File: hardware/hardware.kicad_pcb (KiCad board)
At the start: 4 copper layers, 0 parts

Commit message: atualizando alguns footprints; começando o desenho da placa
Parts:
- added ANT1: PCB_ANT, RF_Antenna:Texas_SWRA117D_2.4GHz_Left, F.Cu at (72.3, 25.4)
- added C1: TBD, Capacitor_SMD:C_0402_1005Metric, F.Cu at (46.5, 20.3)
- added C10: 1uF, Capacitor_SMD:C_0402_1005Metric, F.Cu at (136.1, 82.4)
- added C11: 0.1uF, Capacitor_SMD:C_0402_1005Metric, F.Cu at (46.5, 36.0)
- added C12: 10nF, Capacitor_SMD:C_0402_1005Metric, F.Cu at (136.1, 83.7)
- added C13: 10pF, Capacitor_SMD:C_0402_1005Metric, F.Cu at (49.4, 22.2)
- added C14: 10pF, Capacitor_SMD:C_0402_1005Metric, F.Cu at (49.4, 24.2)
- added C15: 100nF, Capacitor_SMD:C_0805_2012Metric_Pad1.18x1.45mm_HandSolder, F.Cu at (73.5, 44.5)
- added C16: 0.1uF, Capacitor_SMD:C_0402_1005Metric, F.Cu at (49.4, 26.2)
- added C17: 22uF, Capacitor_SMD:C_0603_1608Metric_Pad1.08x0.95mm_HandSolder, F.Cu at (47.2, 52.5)
- added C18: TBD, Capacitor_SMD:C_0402_1005Metric, F.Cu at (49.4, 28.1)
- added C19: TBD, Capacitor_SMD:C_0402_1005Metric, F.Cu at (49.4, 30.1)
- added C2: TBD, Capacitor_SMD:C_0402_1005Metric, F.Cu at (46.5, 22.2)
- added C20: 22uF, Capacitor_SMD:C_0603_1608Metric_Pad1.08x0.95mm_HandSolder, F.Cu at (47.2, 55.0)
- added C21: 22uF, Capacitor_SMD:C_0603_1608Metric_Pad1.08x0.95mm_HandSolder, F.Cu at (47.2, 57.5)
- added C22: 0.1uF, Capacitor_SMD:C_0402_1005Metric, F.Cu at (49.4, 32.1)
- added C23: 0.1uF, Capacitor_SMD:C_0402_1005Metric, F.Cu at (49.4, 34.0)
- added C24: 1uF, Capacitor_SMD:C_0402_1005Metric, F.Cu at (49.4, 36.0)
- added C25: 1uF, Capacitor_SMD:C_0402_1005Metric, F.Cu at (162.4, 129.5)
- added C26: 1uF, Capacitor_SMD:C_0402_1005Metric, F.Cu at (162.3, 125.1)
- added C27: 1uF, Capacitor_SMD:C_0402_1005Metric, F.Cu at (164.0, 125.1)
- added C28: 100nF, Capacitor_SMD:C_0402_1005Metric, F.Cu at (52.2, 26.2)
- added C29: 220nF, Capacitor_SMD:C_0402_1005Metric, F.Cu at (174.8, 129.0)
- added C3: 1uF, Capacitor_SMD:C_0402_1005Metric, F.Cu at (127.0, 87.0)
- added C30: 1uF, Capacitor_SMD:C_0402_1005Metric, F.Cu at (175.3, 123.1)
- added C31: 220nF, Capacitor_SMD:C_0402_1005Metric, F.Cu at (175.7, 124.4)
- added C32: 220nF, Capacitor_SMD:C_0402_1005Metric, F.Cu at (186.8, 129.3)
- added C33: 220nF, Capacitor_SMD:C_0402_1005Metric, F.Cu at (174.8, 127.1)
- added C34: 100nF, Capacitor_SMD:C_0402_1005Metric, F.Cu at (55.1, 20.3)
- added C35: 470nF, Capacitor_SMD:C_0402_1005Metric, F.Cu at (110.2, 103.3)
- added C36: 470nF, Capacitor_SMD:C_0402_1005Metric, F.Cu at (110.2, 105.3)
- added C37: 100nF, Capacitor_SMD:C_0402_1005Metric, F.Cu at (110.2, 107.2)
- added C38: 470uF, Capacitor_SMD:C_0402_1005Metric, F.Cu at (110.2, 109.2)
- added C39: 100nF, Capacitor_SMD:C_0402_1005Metric, F.Cu at (110.2, 111.2)
- added C4: TBD, Capacitor_SMD:C_0402_1005Metric, F.Cu at (46.5, 26.2)
- added C40: 1nF, Capacitor_SMD:C_0402_1005Metric, F.Cu at (110.2, 113.2)
- added C41: 1nF, Capacitor_SMD:C_0402_1005Metric, F.Cu at (110.2, 115.1)
- added C42: 100nF, Capacitor_SMD:C_0402_1005Metric, F.Cu at (55.1, 36.0)
- added C43: 10nF, Capacitor_SMD:C_0402_1005Metric, F.Cu at (113.0, 101.3)
- added C44: 10nF, Capacitor_SMD:C_0402_1005Metric, F.Cu at (113.0, 103.3)
- added C45: 100nF, Capacitor_SMD:C_0402_1005Metric, F.Cu at (58.0, 24.2)
- added C46: 100nF, Capacitor_SMD:C_0402_1005Metric, F.Cu at (58.0, 26.2)
- added C5: 10nF, Capacitor_SMD:C_0402_1005Metric, F.Cu at (128.5, 87.0)
- added C6: 10uF, Capacitor_SMD:C_0805_2012Metric_Pad1.18x1.45mm_HandSolder, F.Cu at (73.5, 38.5)
- added C7: 0.1uF, Capacitor_SMD:C_0402_1005Metric, F.Cu at (130.0, 87.0)
- added C8: 10uF, Capacitor_SMD:C_0805_2012Metric_Pad1.18x1.45mm_HandSolder, F.Cu at (73.5, 41.5)
- added C9: 0.1uF, Capacitor_SMD:C_0402_1005Metric, F.Cu at (134.0, 87.1)
- added D1: LED_ARGB, Connector_PinHeader_1.27mm:PinHeader_1x04_P1.27mm_Vertical_SMD_Pin1Left, F.Cu at (63.4, 29.9)
- added IC1: TAS5760LDAPR, Package_SO:HTSSOP-32-1EP_6.1x11mm_P0.65mm_EP5.2x11mm_Mask4.11x4.36mm_ThermalVias, F.Cu at (169.5, 128.0)
- added J2: Conn_01x04, Connector_PinHeader_1.27mm:PinHeader_1x04_P1.27mm_Vertical, F.Cu at (67.1, 55.2)
- added J3: Conn_01x04, Connector_PinHeader_1.27mm:PinHeader_1x04_P1.27mm_Vertical, F.Cu at (71.3, 55.2)
- added JP1: SolderJumper_2_Open, Jumper:SolderJumper-2_P1.3mm_Open_RoundedPad1.0x1.5mm, F.Cu at (102.3, 119.9)
- added JP2: SolderJumper_2_Open, Jumper:SolderJumper-2_P1.3mm_Open_RoundedPad1.0x1.5mm, F.Cu at (102.3, 123.4)
- added JP3: SolderJumper_2_Open, Jumper:SolderJumper-2_P1.3mm_Open_RoundedPad1.0x1.5mm, F.Cu at (102.3, 127.0)
- added JP4: SolderJumper_2_Open, Jumper:SolderJumper-2_P1.3mm_Open_RoundedPad1.0x1.5mm, F.Cu at (102.3, 130.5)
- added L1: TBD, Inductor_SMD:L_0402_1005Metric, F.Cu at (60.9, 38.0)
- added L2: TBD, Inductor_SMD:L_0402_1005Metric, F.Cu at (60.9, 40.0)
- added L3: 2.0nH (0.1nH), Inductor_SMD:L_0402_1005Metric, F.Cu at (132.0, 86.6)
- added L4: 2.2uH, Inductor_SMD:L_TDK_VLS6045EX_VLS6045AF, F.Cu at (71.3, 30.1)
- added L5: 10uH, Inductor_SMD:L_0402_1005Metric, F.Cu at (116.0, 125.0)
- added L6: 10uH, Inductor_SMD:L_0402_1005Metric, F.Cu at (116.0, 127.0)
- added LS1: 4R, Connector_PinSocket_2.54mm:PinSocket_2x01_P2.54mm_Vertical_SMD, F.Cu at (125.2, 132.3)
- added R1: 49.9K, Resistor_SMD:R_0402_1005Metric, F.Cu at (60.9, 47.9)
- added R10: 10K, Resistor_SMD:R_0201_0603Metric_Pad0.64x0.40mm_HandSolder, F.Cu at (60.9, 51.6)
- added R11: 10K, Resistor_SMD:R_0201_0603Metric_Pad0.64x0.40mm_HandSolder, F.Cu at (163.8, 126.4)
- added R12: 10K, Resistor_SMD:R_0201_0603Metric_Pad0.64x0.40mm_HandSolder, F.Cu at (163.9, 128.4)
- added R13: 10K, Resistor_SMD:R_0201_0603Metric_Pad0.64x0.40mm_HandSolder, F.Cu at (163.9, 129.6)
- added R14: R, Resistor_SMD:R_0201_0603Metric_Pad0.64x0.40mm_HandSolder, F.Cu at (163.9, 127.6)
- added R15: R, Resistor_SMD:R_0201_0603Metric_Pad0.64x0.40mm_HandSolder, F.Cu at (163.8, 132.2)
- added R16: 10K, Resistor_SMD:R_0201_0603Metric_Pad0.64x0.40mm_HandSolder, F.Cu at (60.9, 58.6)
- added R17: 560R, Resistor_SMD:R_0402_1005Metric, F.Cu at (66.7, 44.0)
- added R18: 560R, Resistor_SMD:R_0402_1005Metric, F.Cu at (66.7, 46.0)
- added R19: 560R, Resistor_SMD:R_0402_1005Metric, F.Cu at (66.7, 47.9)
- added R2: 49.9K, Resistor_SMD:R_0402_1005Metric, F.Cu at (63.8, 38.0)
- added R20: 10K, Resistor_SMD:R_0201_0603Metric_Pad0.64x0.40mm_HandSolder, F.Cu at (63.7, 49.8)
- added R21: 1K, Resistor_SMD:R_0402_1005Metric, F.Cu at (69.6, 38.0)
- added R22: 10K, Resistor_SMD:R_0201_0603Metric_Pad0.64x0.40mm_HandSolder, F.Cu at (63.7, 51.6)
- added R23: 3.3R, Resistor_SMD:R_0402_1005Metric, F.Cu at (124.7, 121.1)
- added R24: 3.3R, Resistor_SMD:R_0402_1005Metric, F.Cu at (124.7, 123.1)
- added R25: 1K, Resistor_SMD:R_0402_1005Metric, F.Cu at (69.6, 44.0)
- added R26: 10K, Resistor_SMD:R_0201_0603Metric_Pad0.64x0.40mm_HandSolder, F.Cu at (63.7, 53.3)
- added R27: 10K, Resistor_SMD:R_0201_0603Metric_Pad0.64x0.40mm_HandSolder, F.Cu at (63.7, 55.1)
- added R3: 49.9K, Resistor_SMD:R_0402_1005Metric, F.Cu at (63.8, 40.0)
- added R4: 49.9K, Resistor_SMD:R_0402_1005Metric, F.Cu at (63.8, 42.0)
- added R5: 10K, Resistor_SMD:R_0201_0603Metric_Pad0.64x0.40mm_HandSolder, F.Cu at (60.9, 49.8)
- added R6: 0R, Resistor_SMD:R_0402_1005Metric, F.Cu at (63.8, 44.0)
- added R7: TBD, Resistor_SMD:R_0402_1005Metric, F.Cu at (63.8, 46.0)
- added R8: 499R, Resistor_SMD:R_0402_1005Metric, F.Cu at (63.8, 47.9)
- added R9: 33.2K, Resistor_SMD:R_0402_1005Metric, F.Cu at (66.7, 38.0)
- added SW1: SW_Push, Button_Switch_SMD:SW_SPST_PTS810, F.Cu at (41.7, 21.6)
- added SW2: SW_Push, Button_Switch_SMD:SW_SPST_PTS810, F.Cu at (41.7, 26.4)
- added SW3: SW_Push, Button_Switch_SMD:SW_SPST_PTS810, F.Cu at (41.7, 31.1)
- added SW4: SW_Push, Button_Switch_SMD:SW_SPST_PTS810, F.Cu at (41.7, 35.9)
- added SW5: SW_Push, Button_Switch_SMD:SW_SPST_PTS810, F.Cu at (41.7, 40.6)
- added SW6: SW_Push, Button_Switch_SMD:SW_SPST_PTS810, F.Cu at (41.7, 45.4)
- added U1: TPS563200, Package_TO_SOT_SMD:SOT-23-6, F.Cu at (40.9, 50.2)
- added U2: ESP32-S3, Package_DFN_QFN:QFN-56-1EP_7x7mm_P0.4mm_EP4x4mm, F.Cu at (139.0, 88.6)
- added Y1: 40MHz, Crystal:Crystal_SMD_2520-4Pin_2.5x2.0mm, F.Cu at (40.5, 54.4)

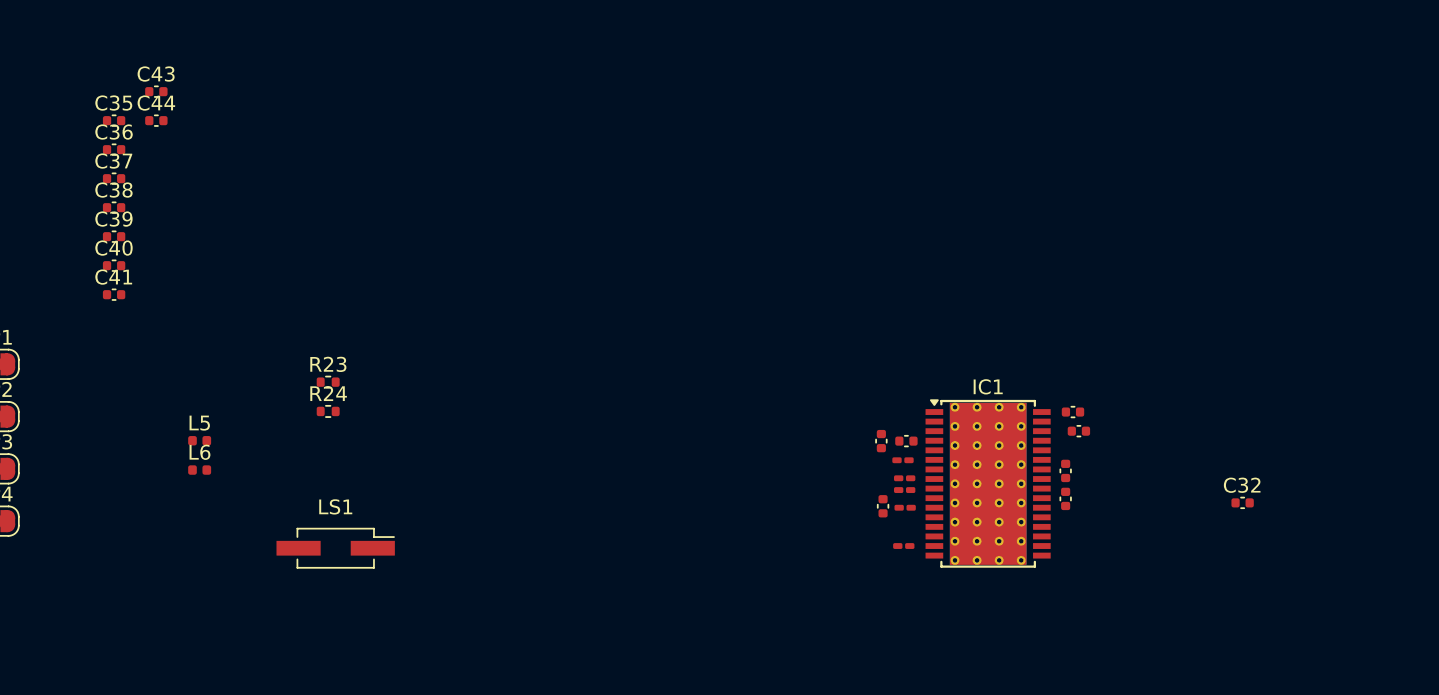
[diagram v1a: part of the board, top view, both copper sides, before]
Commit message: RTC footprint; removed 2 buttons, an will remove more stuff to get the USB back
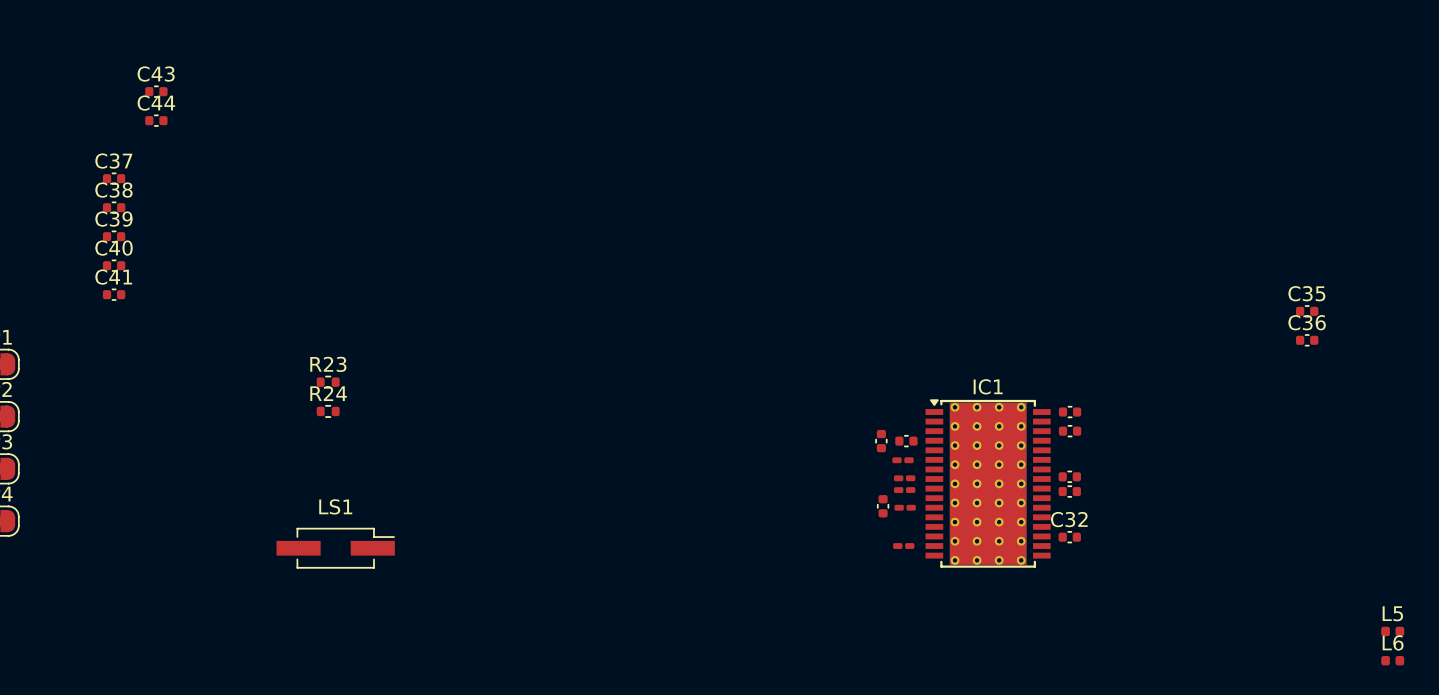
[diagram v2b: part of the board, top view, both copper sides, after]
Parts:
- moved C35 82.1 mm to (191.2, 116.3)
- moved C36 82.1 mm to (191.2, 118.2)
- moved L5 82.1 mm to (197.0, 138.0)
- moved L6 82.1 mm to (197.0, 140.0)
- moved C32 12.0 mm to (175.1, 131.6)
- moved C31 0.60 mm to (175.1, 124.4)
- moved C29 0.57 mm to (175.1, 128.5), turned to 180 degrees
- moved C33 0.49 mm to (175.1, 127.5), turned to 180 degrees
- moved C30 0.20 mm to (175.1, 123.1)

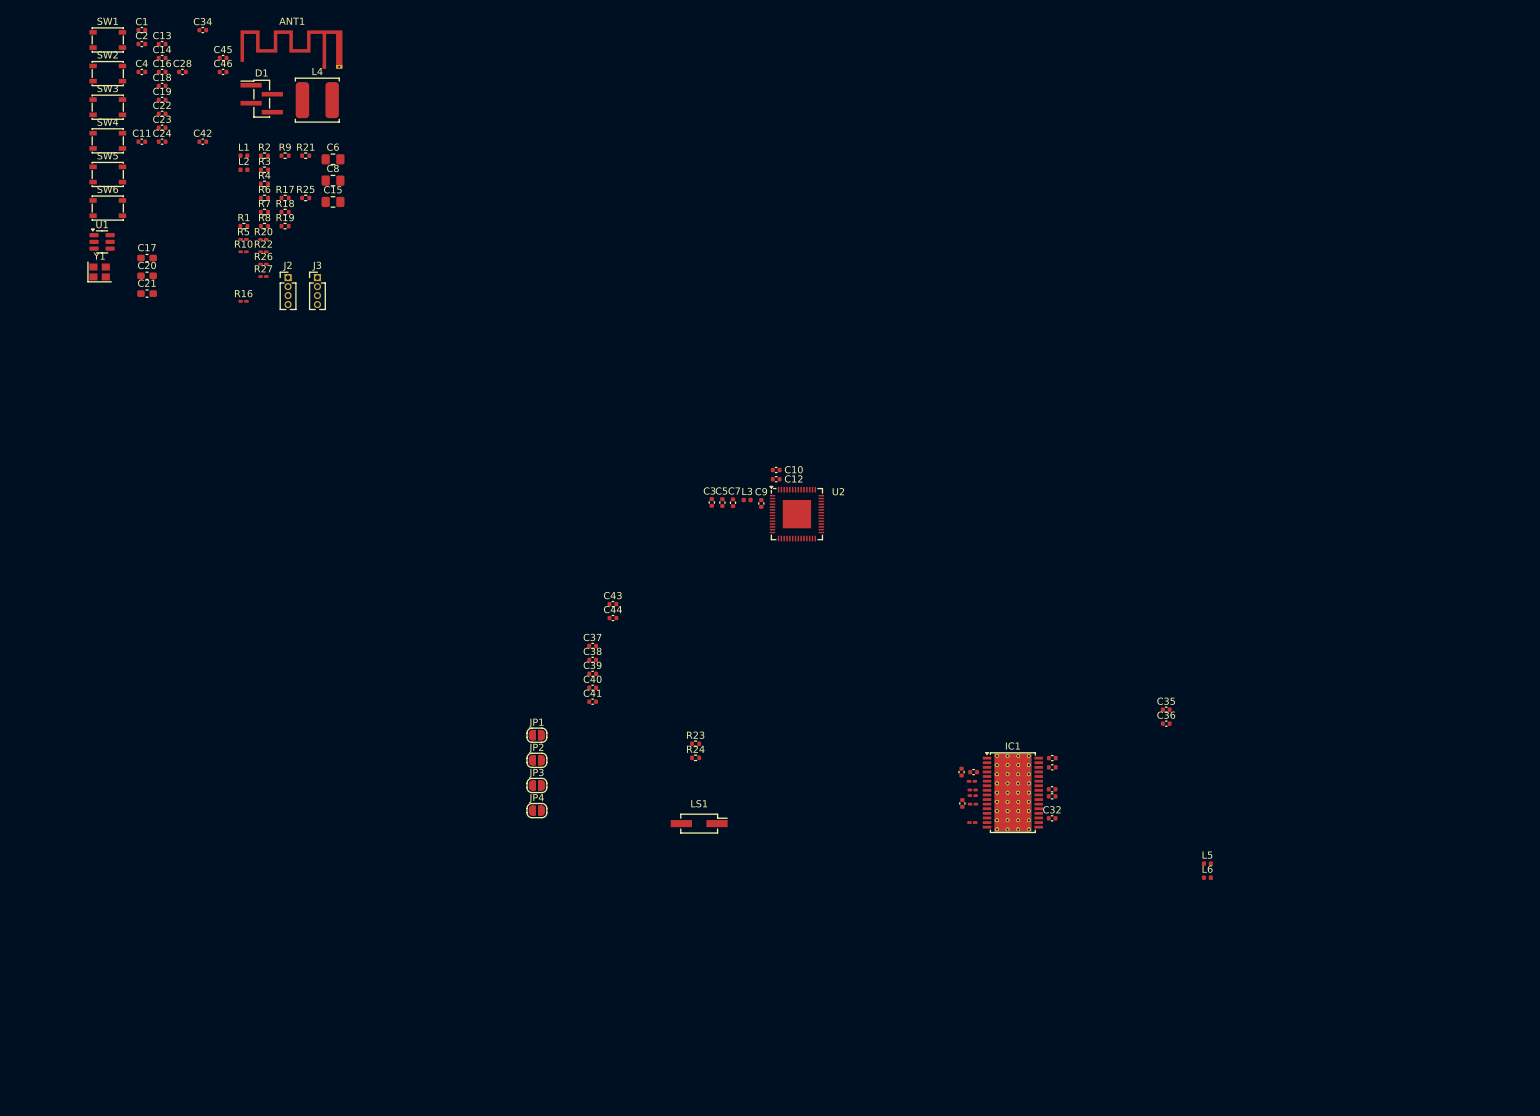
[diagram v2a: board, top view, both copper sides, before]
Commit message: sound components placed - there were some differences between layout and schematic on the amplifier documentation. They are emphasized by squares on schematic
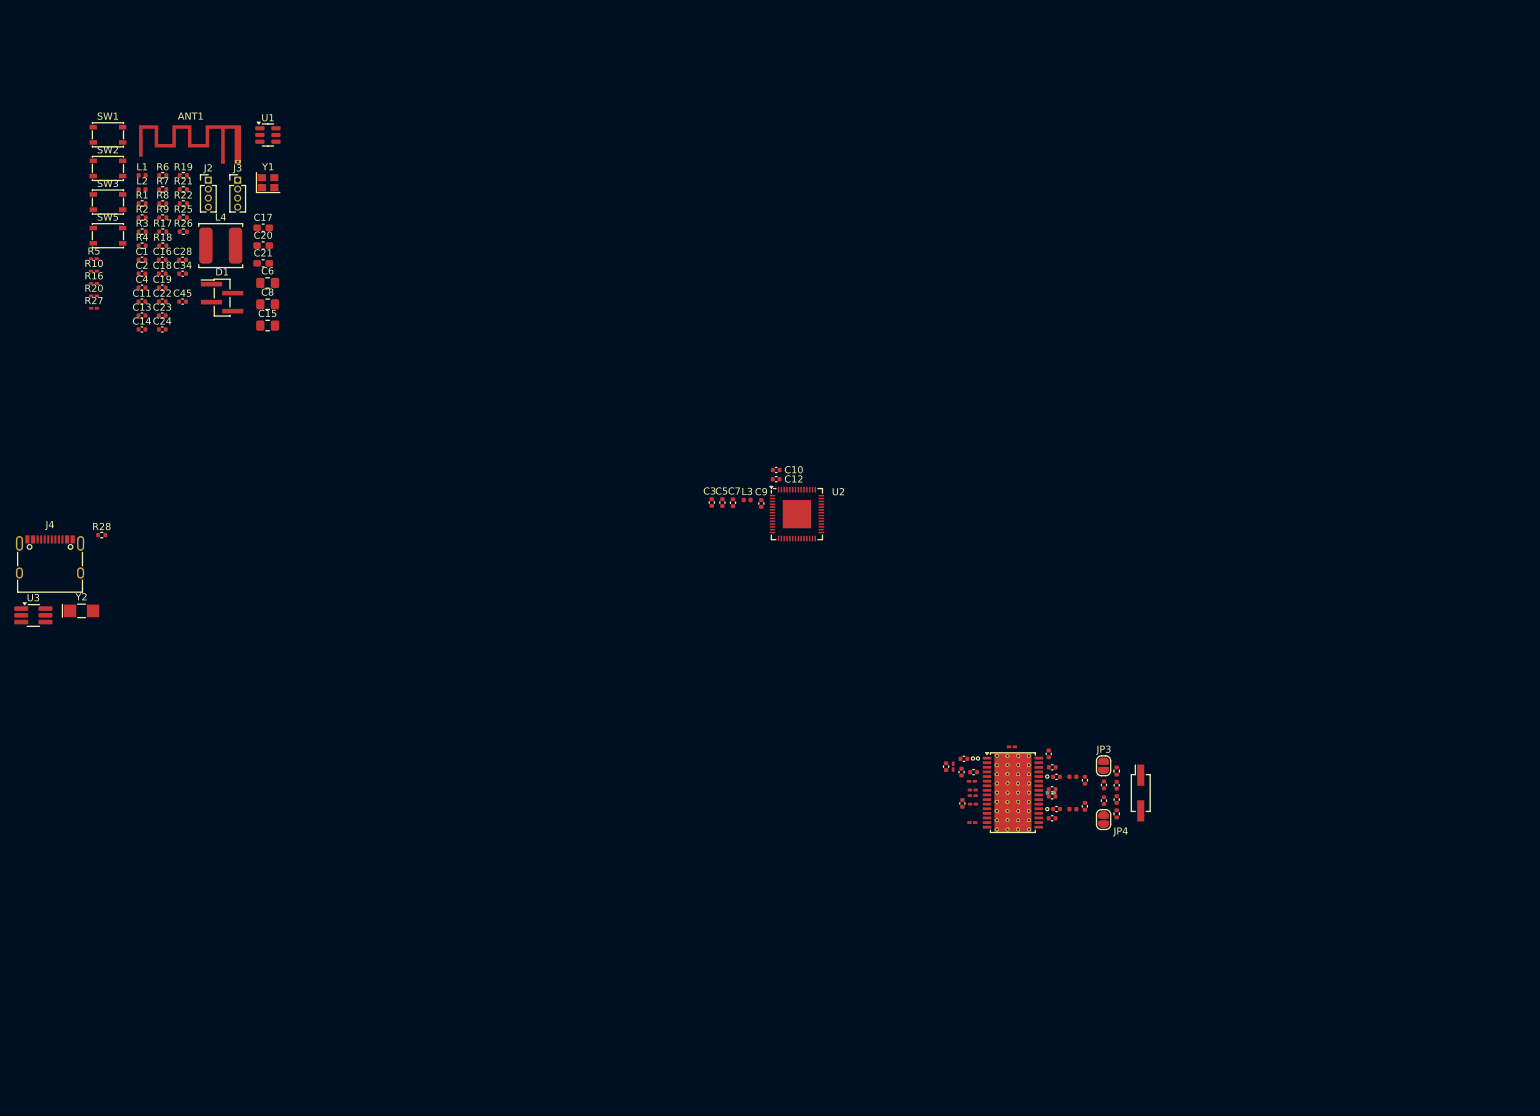
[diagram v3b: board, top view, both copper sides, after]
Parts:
- removed JP1, JP2: SolderJumper_2_Open, Jumper:SolderJumper-2_P1.3mm_Open_RoundedPad1.0x1.5mm
- removed SW4, SW6: SW_Push, Button_Switch_SMD:SW_SPST_PTS810
- added J4: USB-C, Connector_USB:USB_C_Receptacle_XKB_U262-16XN-4BVC11, F.Cu at (33.5, 95.9)
- added R28: 0R, Resistor_SMD:R_0402_1005Metric, F.Cu at (40.8, 91.6)
- added R29: 47R, Resistor_SMD:R_0201_0603Metric_Pad0.64x0.40mm_HandSolder, F.Cu at (161.1, 124.3)
- added R30: 10K, Resistor_SMD:R_0201_0603Metric_Pad0.64x0.40mm_HandSolder, F.Cu at (169.4, 121.5)
- added U3: USBLC6-2SC6, Package_TO_SOT_SMD:TSOT-23-6_HandSoldering, F.Cu at (31.2, 102.9)
- added Y2: ABS07-166-32.768KHZ-T, Crystal:Crystal_SMD_MicroCrystal_CC7V-T1A-2Pin_3.2x1.5mm_HandSoldering, F.Cu at (38.0, 102.3)
- C38: moved to B.Cu
- C42, C46: value 100nF -> 1uF
- R22: value 10K -> 5K1; footprint Resistor_SMD:R_0201_0603Metric_Pad0.64x0.40mm_HandSolder -> Resistor_SMD:R_0402_1005Metric
- R26: value 10K -> 0R; footprint Resistor_SMD:R_0201_0603Metric_Pad0.64x0.40mm_HandSolder -> Resistor_SMD:R_0402_1005Metric
- moved C46 141.6 mm to (160.1, 124.3), turned to 90 degrees
- moved C42 138.4 mm to (162.6, 123.2)
- moved JP3 80.1 mm to (182.3, 124.2), turned to 90 degrees
- moved JP4 80.1 mm to (182.3, 131.8), turned to 90 degrees
- moved C44 75.6 mm to (184.2, 128.9), turned to 90 degrees
- moved C43 75.6 mm to (184.2, 126.9), turned to 90 degrees
- moved C41 73.6 mm to (182.4, 129.1), turned to 90 degrees
- moved C40 73.5 mm to (182.4, 126.9), turned to 90 degrees
- moved C39 68.3 mm to (175.7, 130.3), turned to 180 degrees
- moved C37 68.1 mm to (175.7, 125.8), turned to 180 degrees
- moved C38 67.4 mm to (174.9, 128.0), turned to 180 degrees
- moved LS1 62.5 mm to (187.6, 128.0), turned to 90 degrees
- moved R24 60.0 mm to (184.2, 131.0), turned to 90 degrees
- moved R23 59.6 mm to (184.2, 124.9), turned to 90 degrees
- moved C13 38.5 mm to (46.5, 60.6)
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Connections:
- C28 pad 1: BT_N -> BT_L
- C34 pad 1: BT_S -> BT_R
- C40 pad 2: Net-(JP1-A) -> Net-(JP3-A)
- C41 pad 1: Net-(JP2-B) -> Net-(JP4-B)
- C42 pad 1: BT_E -> GND
- C42 pad 2: 3V3 -> 8V
- C46 pad 1: BT_W -> Net-(IC1-SFT_CLIP)
- C46 pad 2: 3V3 -> GND
- IC1 pad 2: Net-(IC1-GVDD_REG) -> Net-(IC1-SFT_CLIP)
- IC1 pad 6: Net-(IC1-~{SPK_FAULT}) -> AUDIO_FAULT
- R11 pad 1: Net-(IC1-~{SPK_FAULT}) -> 3V3
- R11 pad 2: 3V3 -> AUDIO_FAULT
- R16 pad 1: BT_N -> BT_L
- R20 pad 1: BT_S -> BT_R
- R22 pad 1: BT_E -> /CC1
- R22 pad 2: GPIO_45_46 -> GND
- R26 pad 1: BT_W -> Net-(U2-GPIO19/USB_D-)
- R26 pad 2: GPIO_45_46 -> USB_DN
- SW1 pad 2: BT_N -> BT_L
- SW2 pad 2: BT_S -> BT_R
- U2 pad 19: unconnected-(U2-GPIO14-Pad19) -> BT_L
- U2 pad 23: BT_N -> Display_SDA
- U2 pad 24: BT_S -> Display_SCL
- U2 pad 25: BT_E -> Net-(U2-GPIO19/USB_D-)
- U2 pad 26: BT_W -> Net-(U2-GPIO20/USB_D+)
- U2 pad 27: Display_SDA -> BT_R
- U2 pad 28: Display_SCL -> unconnected-(U2-SPICS1-Pad28)
- U2 pad 6: 3V3 -> AUDIO_FAULT
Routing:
- net (no net): vias 0 -> 4
